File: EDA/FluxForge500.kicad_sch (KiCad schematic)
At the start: 55 parts, among them Q1 SFG019N100C3, Q2 SFG019N100C3, Q3 SFG019N100C3, Q4 SFG019N100C3, U1 LM5176PWPR, U2 STGAP2SCMTR, U3 STGAP2SCMTR, U4 STGAP2SCMTR, U5 STGAP2SCMTR

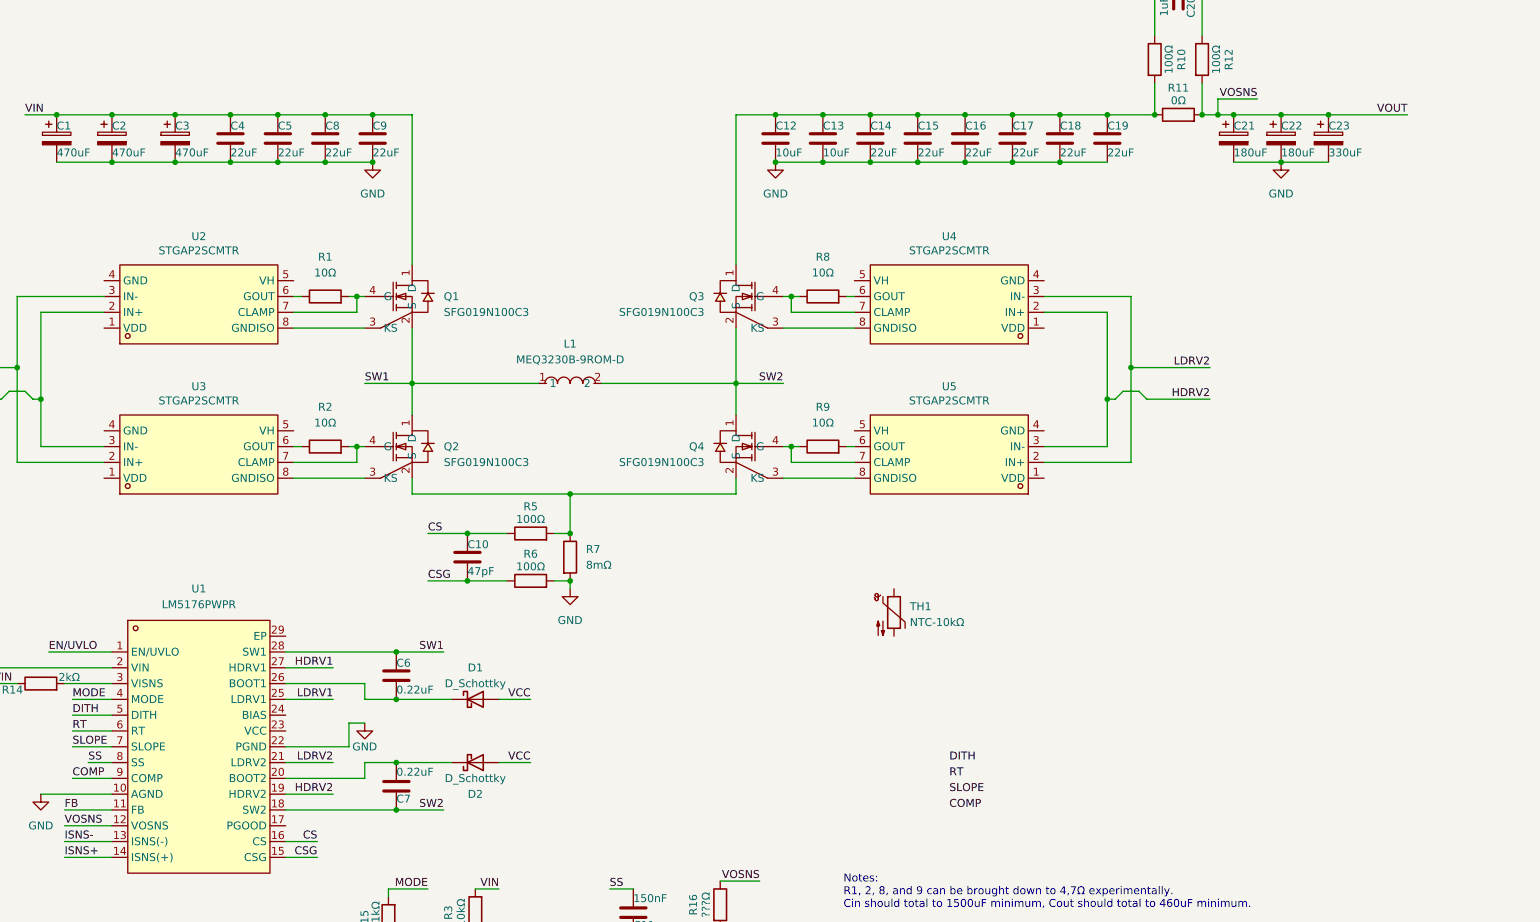
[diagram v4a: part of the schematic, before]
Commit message: Added ADC and a 2 channel fan controller for cooling.
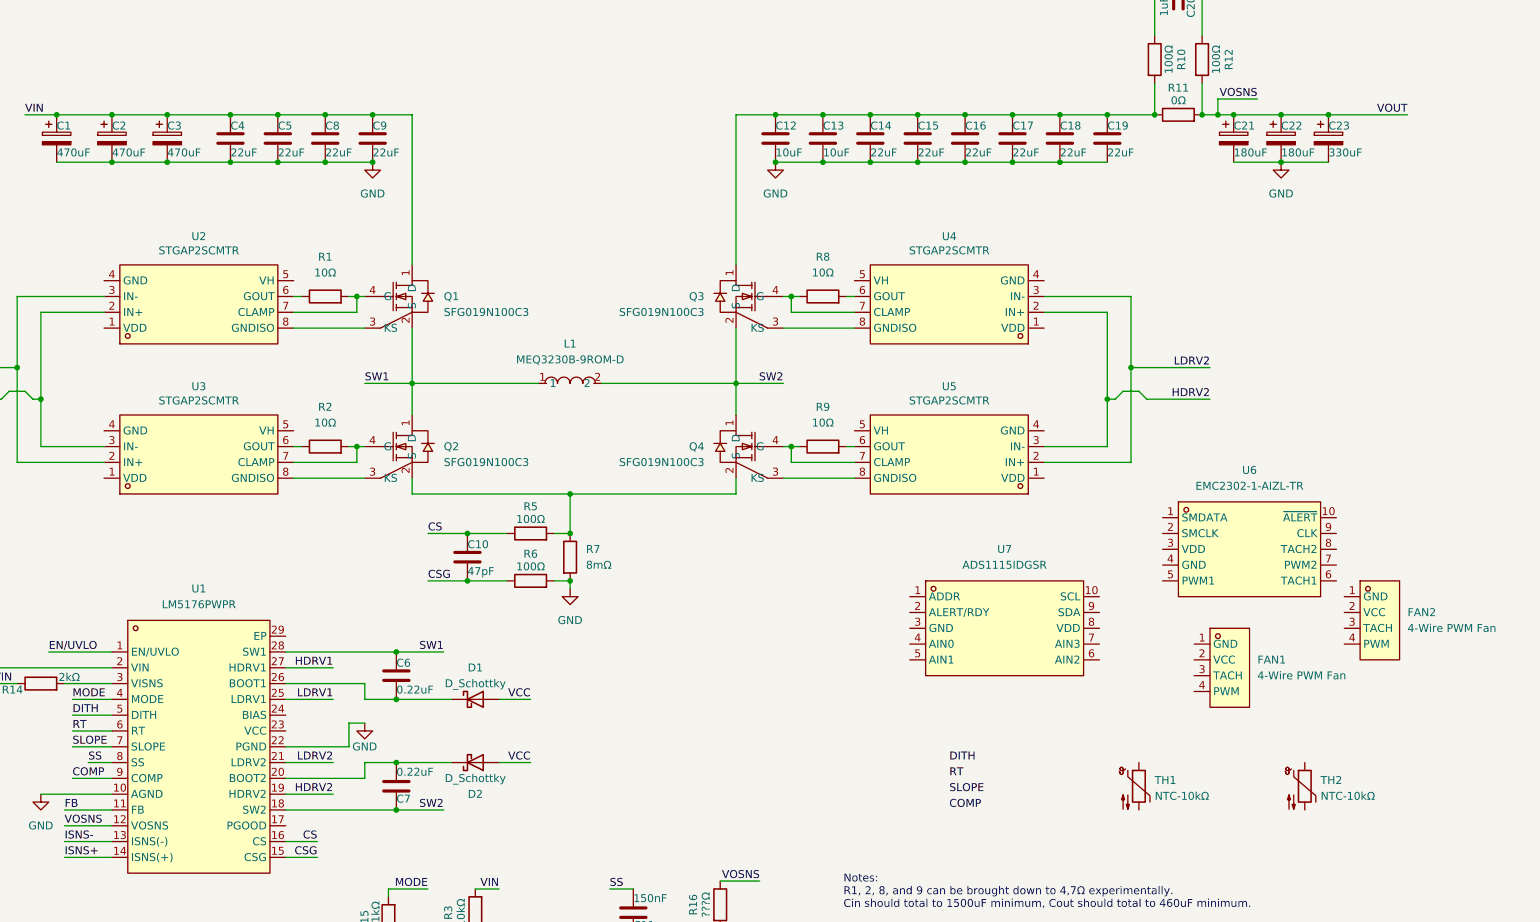
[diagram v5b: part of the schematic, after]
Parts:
- added FAN1, FAN2: 4-Wire PWM Fan, FluxForge500-lib:CONN-TH_47053-1000, symbol FluxForge500:4-Wire PWM Fan
- added TH2: NTC-10kΩ, FluxForge500-lib:NTC-TH_L8.8-W5.5-P1.50-D0.2, symbol FluxForge500:Thermistor_NTC-NTCALUG03A103H
- added U6: EMC2302-1-AIZL-TR, FluxForge500-lib:MSOP-10_L3.0-W3.0-P0.50-LS4.9-BL, symbol FluxForge500:EMC2302-1-AIZL-TR
- added U7: ADS1115IDGSR, FluxForge500-lib:VSSOP-10_L3.0-W3.0-P0.50-LS5.0-BL, symbol FluxForge500:ADS1115IDGSR
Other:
- moved on the sheet: C3, TH1

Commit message: Removed ADC in favor of bult in of chosen low-power STM32 MCU
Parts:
- removed U7: ADS1115IDGSR, FluxForge500-lib:VSSOP-10_L3.0-W3.0-P0.50-LS5.0-BL, symbol FluxForge500:ADS1115IDGSR
- added U6: STM32U073CBT6, FluxForge500-lib:LFQFP-48_L7.0-W7.0-P0.50-LS9.0-BL, symbol FluxForge500:STM32U073CBT6
- renumbered C24 to C1, C7 to C10, C10 to C11, C11 to C12, C12 to C13, C13 to C14, C14 to C15, C15 to C16, C16 to C17, C17 to C18, C18 to C19, C1 to C2, C19 to C20, C20 to C21, C21 to C22, C22 to C23, C23 to C24, C2 to C3, C3 to C4, C4 to C5, C5 to C6, C8 to C7, C9 to C8, C6 to C9, D3 to D1, D1 to D2, D2 to D3, R13 to R1, R7 to R10, R16 to R11, R17 to R12, R8 to R13, R9 to R14, R10 to R15, R11 to R16, R12 to R17, R14 to R2, R1 to R3, R2 to R4, R15 to R5, R3 to R6, R4 to R7, R5 to R8, R6 to R9, U2 to U1, U3 to U2, U1 to U3, U6 to U7
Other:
- moved on the sheet: FAN1, FAN2, TH1, TH2, U7
